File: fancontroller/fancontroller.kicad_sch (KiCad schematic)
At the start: 42 parts, among them J1 Power, J2 Serial Conn, M1 FAN0, M2 FAN0, M3 FAN0, M4 FAN0, M5 FAN0, M6 FAN0, Q1 AO3400A, Q10 AO3401A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

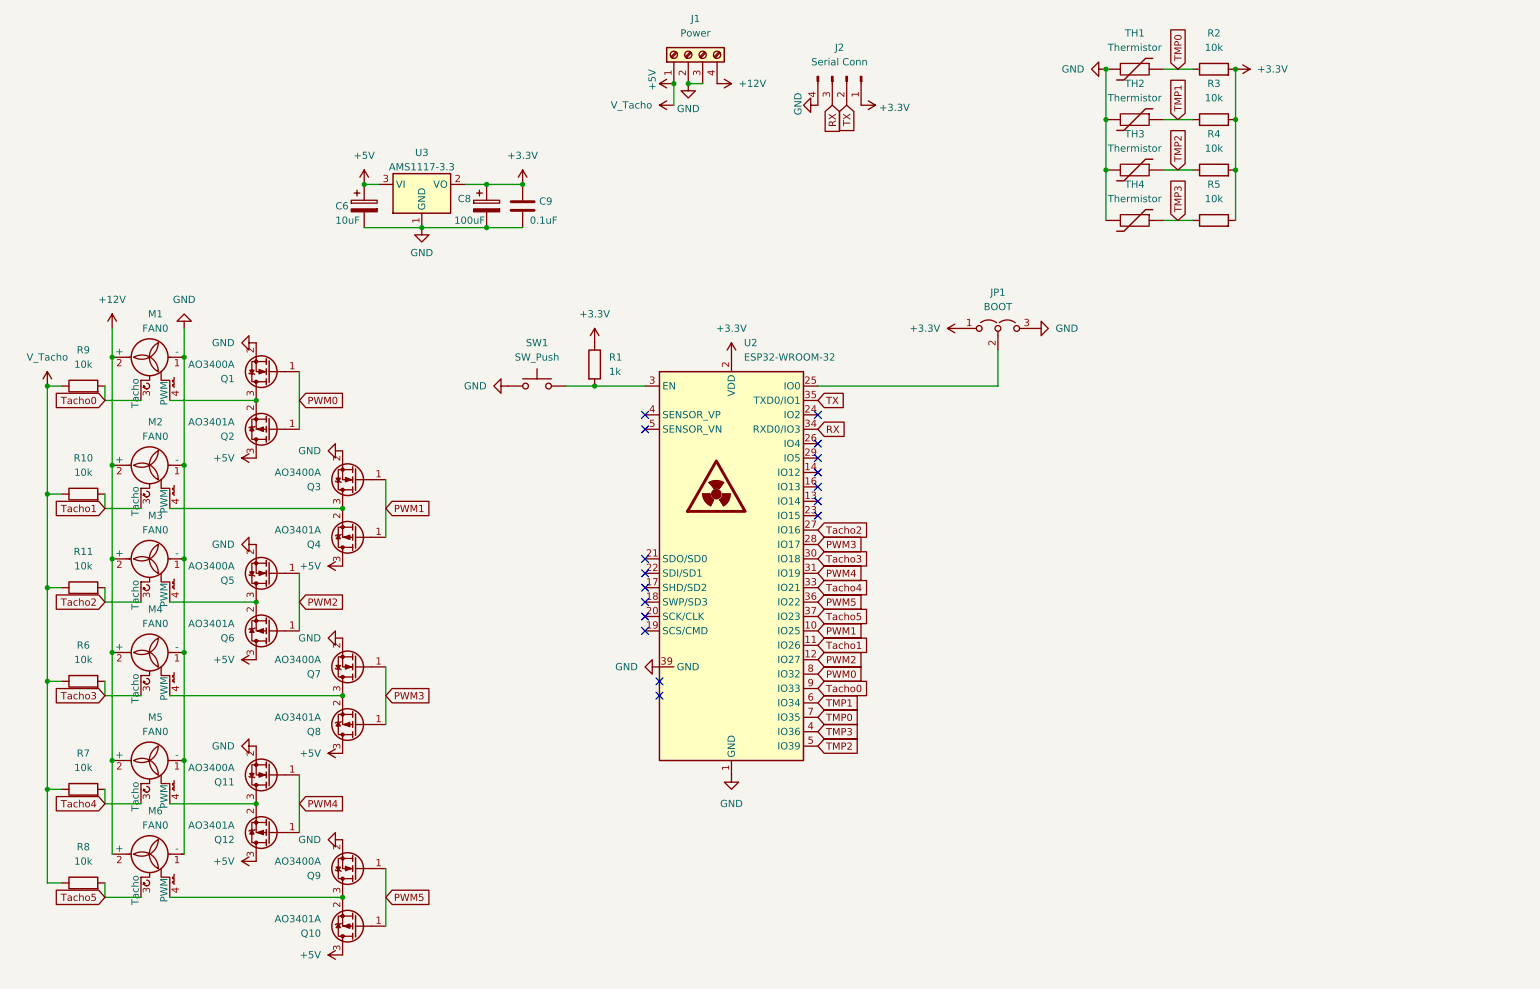
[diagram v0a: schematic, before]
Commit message: Break up into schematics and add USB-C programming interface
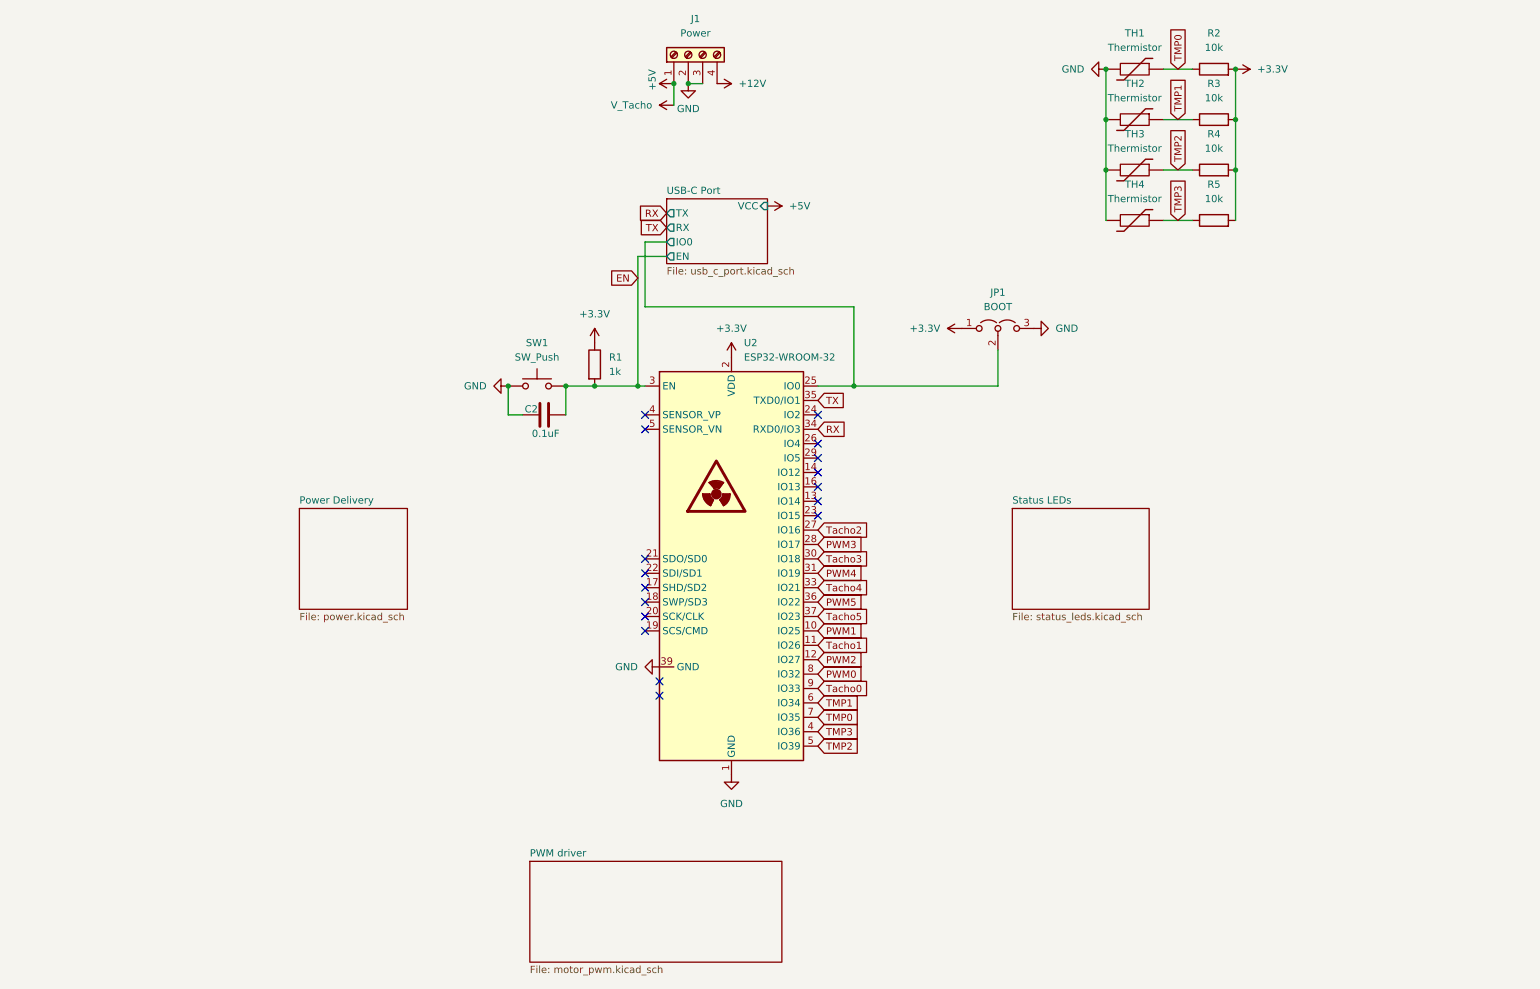
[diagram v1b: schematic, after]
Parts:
- removed C6: 10uF, Capacitor_SMD:C_0805_2012Metric, symbol Device:C_Polarized
- removed C8: 100uF, Capacitor_SMD:CP_Elec_10x10, symbol Device:C_Polarized
- removed C9: 0.1uF, Capacitor_SMD:C_0805_2012Metric, symbol Device:C
- removed J2: Serial Conn, Connector_PinHeader_2.54mm:PinHeader_1x04_P2.54mm_Horizontal, symbol Connector:Conn_01x04_Pin
- removed M1, M2, M3, M4, M5, M6: FAN0, Connector:FanPinHeader_1x04_P2.54mm_Vertical, symbol Motor:Fan_Tacho_PWM
- removed Q1, Q11, Q3, Q5, Q7, Q9: AO3400A, Package_TO_SOT_SMD:SOT-23, symbol Transistor_FET:AO3400A
- removed Q10, Q12, Q2, Q4, Q6, Q8: AO3401A, Package_TO_SOT_SMD:SOT-23, symbol Transistor_FET:AO3401A
- removed R10, R11, R6, R7, R8, R9: 10k, Resistor_SMD:R_0805_2012Metric, symbol Device:R
- removed U3: AMS1117-3.3, Package_TO_SOT_SMD:SOT-223-3_TabPin2, symbol Regulator_Linear:AMS1117-3.3
- added C2: 0.1uF, symbol Device:C
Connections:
- net GND: now also C2.2
- net EN: now reaches R1.2, SW1.2, U2.3 (EN)
- net EN: now also C2.1
- net USB-C Port/IO0: now reaches JP1.2 (C), U2.25 (IO0)
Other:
- added sheet PWM driver (motor_pwm.kicad_sch)
- added sheet Power Delivery (power.kicad_sch)
- added sheet Status LEDs (status_leds.kicad_sch)
- added sheet USB-C Port (usb_c_port.kicad_sch)

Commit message: Restructure Fan drivers into separate modules and rework USB-C
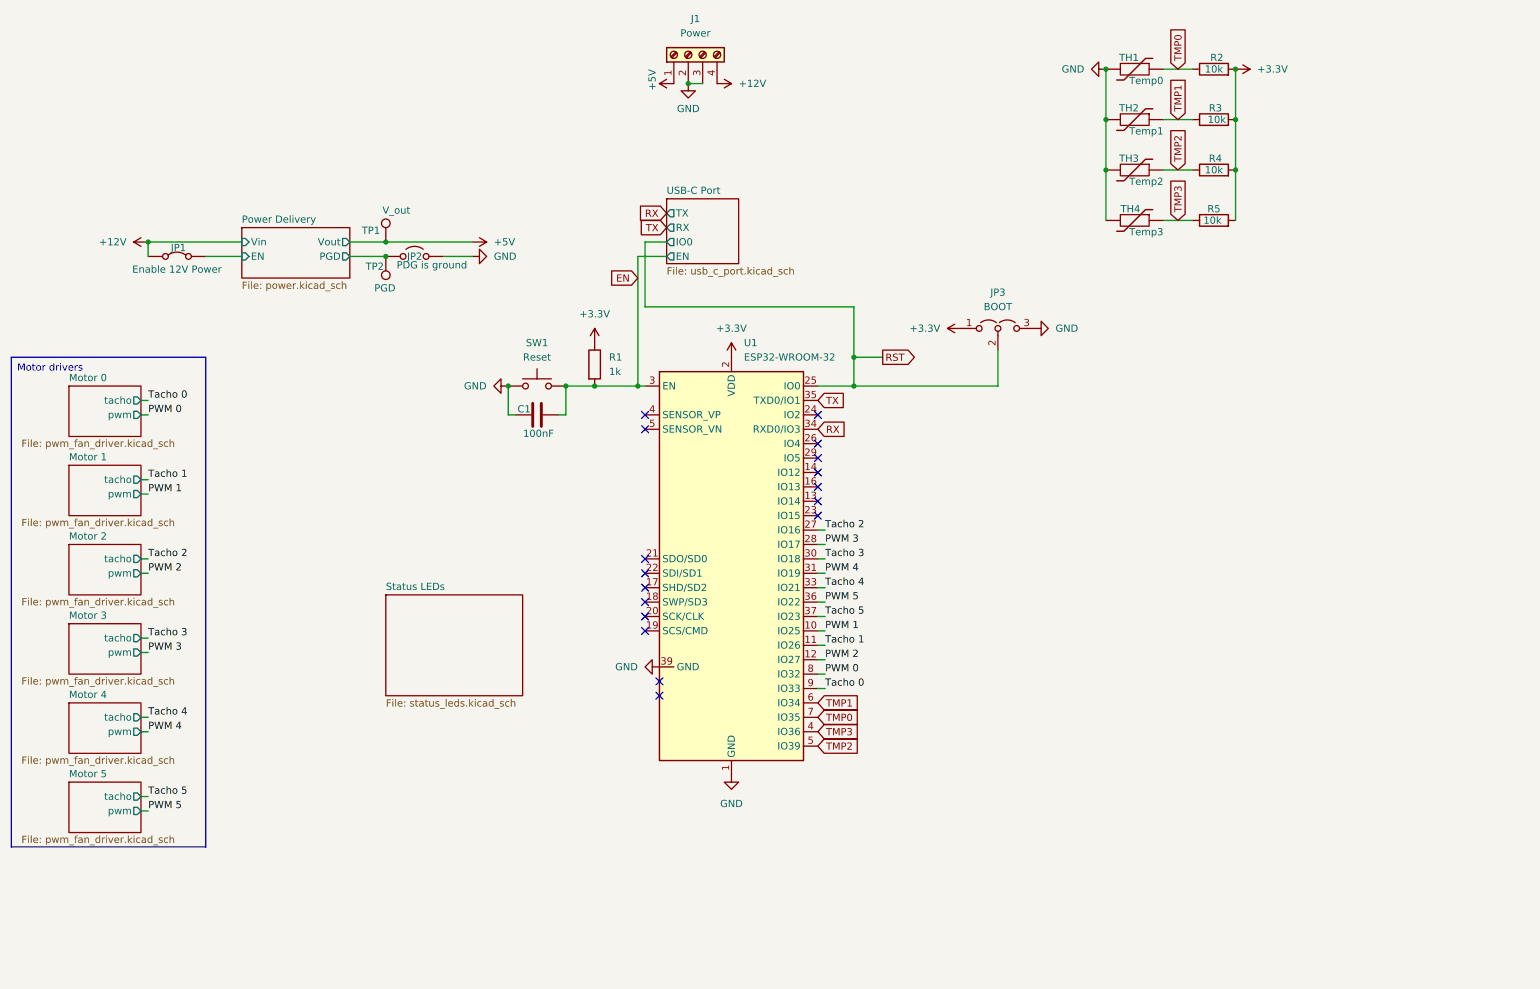
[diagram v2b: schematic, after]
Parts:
- added JP1: Enable 12V Power, symbol Jumper:Jumper_2_Bridged
- added JP2: PDG is ground, symbol Jumper:Jumper_2_Open
- added TP1: V_out, symbol Connector:TestPoint
- added TP2: PGD, symbol Connector:TestPoint
- C1: renamed from C2; value 0.1uF -> 100nF; footprint (none) -> Capacitor_SMD:C_0805_2012Metric; LCSC Part # (none) -> C1525
- SW1: value SW_Push -> Reset
- TH1: value Thermistor -> Temp0
- TH2: value Thermistor -> Temp1
- TH3: value Thermistor -> Temp2
- TH4: value Thermistor -> Temp3
- U1: renamed from U2; LCSC Part # (none) -> C2973652
- renumbered JP1 to JP3
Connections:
- net +12V: now also JP1.1 (A)
- net +5V: now also TP1.1
- net GND: now also JP2.2 (B)
- net PWM0 renamed PWM 0
- net PWM1 renamed PWM 1
- net PWM2 renamed PWM 2
- net PWM3 renamed PWM 3
- net PWM4 renamed PWM 4
- net PWM5 renamed PWM 5
- net Tacho0 renamed Tacho 0
- net Tacho1 renamed Tacho 1
- net Tacho2 renamed Tacho 2
- net Tacho3 renamed Tacho 3
- net Tacho4 renamed Tacho 4
- net Tacho5 renamed Tacho 5
- net USB-C Port/IO0 renamed RST
- new net Power Delivery/EN: JP1.2 (B)
- new net Power Delivery/PGD: JP2.1 (A), TP2.1
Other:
- removed sheet PWM driver
- added sheet Motor 0 (pwm_fan_driver.kicad_sch)
- added sheet Motor 1 (pwm_fan_driver.kicad_sch)
- added sheet Motor 2 (pwm_fan_driver.kicad_sch)
- added sheet Motor 3 (pwm_fan_driver.kicad_sch)
- added sheet Motor 4 (pwm_fan_driver.kicad_sch)
- added sheet Motor 5 (pwm_fan_driver.kicad_sch)
- sheet Power Delivery ports: added EN, PGD, Vin, Vout; removed none
- sheet USB-C Port ports: added none; removed VCC
- moved on the sheet: C1

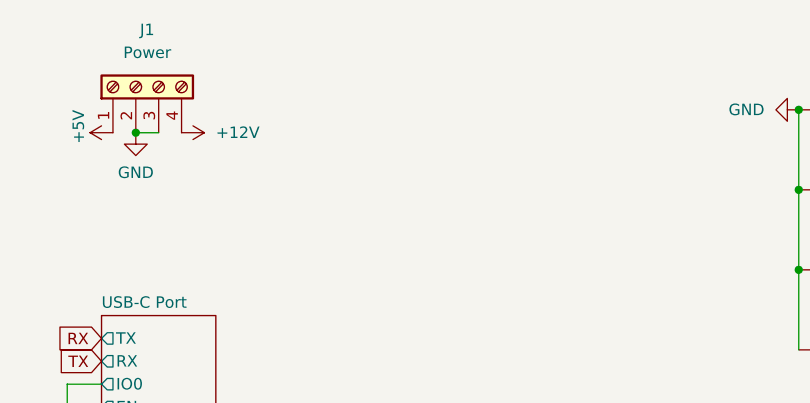
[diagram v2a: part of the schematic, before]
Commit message: Improve footprints and do massive overhaul for part numbering for better future order
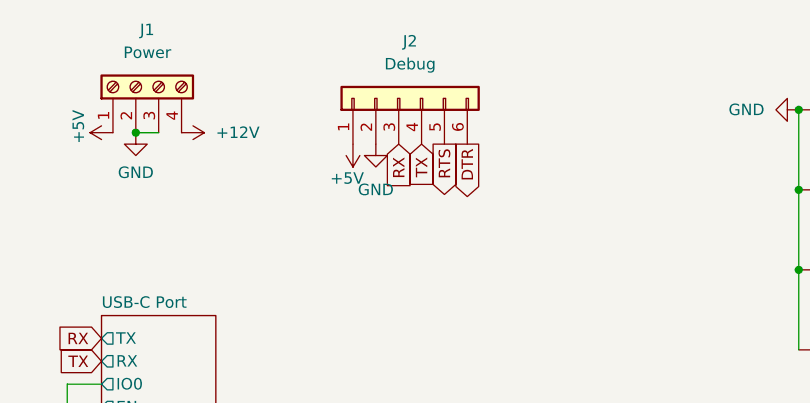
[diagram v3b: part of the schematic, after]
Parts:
- added J2: Debug, Connector_PinHeader_2.54mm:PinHeader_1x06_P2.54mm_Vertical, symbol Connector_Generic:Conn_01x06
- JP1, JP2: footprint (none) -> Connector_PinHeader_2.54mm:PinHeader_1x02_P2.54mm_Vertical
- TP1, TP2: footprint (none) -> TestPoint:TestPoint_Pad_2.5x2.5mm
- U1: footprint RF_Module:ESP32-WROOM-32 -> PCM_Espressif:ESP32-WROOM-32E
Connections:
- net +5V: now also J2.1 (Pin_1)
- net GND: now also J2.2 (Pin_2)
- net RX: now also J2.3 (Pin_3)
- net TX: now also J2.4 (Pin_4)
- new net DTR: J2.6 (Pin_6)
- new net RTS: J2.5 (Pin_5)
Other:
- company: (none) -> DJ-Bauer
- title: (none) -> ESP-Fancontroller

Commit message: Begin placing parts for v0.1 layout
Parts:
- J1: footprint Connector_PinHeader_2.54mm:PinHeader_1x04_P2.54mm_Horizontal -> Connector_PinHeader_2.54mm:PinHeader_1x04_P2.54mm_Vertical
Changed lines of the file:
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@@
 			)
 		)
-		(property "Footprint" "Connector_PinHeader_2.54mm:PinHeader_1x04_P2.54mm_Horizontal"
+		(property "Footprint" "Connector_PinHeader_2.54mm:PinHeader_1x04_P2.54mm_Vertical"
 			(at 133.35 29.21 0)
 			(effects

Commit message: edit schematic
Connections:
- net PWM 0: now also U1.12 (IO27); no longer U1.8 (IO32)
- net PWM 2: now also U1.8 (IO32); no longer U1.12 (IO27)
- net PWM 3: now also U1.36 (IO22); no longer U1.28 (IO17)
- net PWM 5: now also U1.27 (IO16); no longer U1.36 (IO22)
- net Tacho 0: now also U1.11 (IO26); no longer U1.9 (IO33)
- net Tacho 1: now also U1.9 (IO33); no longer U1.11 (IO26)
- net Tacho 2: now also U1.37 (IO23); no longer U1.27 (IO16)
- net Tacho 5: now also U1.28 (IO17); no longer U1.37 (IO23)
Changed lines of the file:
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@@
 	)
 	(label "Tacho 5"
-		(at 157.48 128.27 0)
+		(at 157.48 115.57 0)
 		(fields_autoplaced yes)
 		(effects
@@
 	)
 	(label "PWM 5"
-		(at 157.48 125.73 0)
+		(at 157.48 113.03 0)
 		(fields_autoplaced yes)
 		(effects
@@
 	)
 	(label "PWM 0"
-		(at 157.48 138.43 0)
+		(at 157.48 135.89 0)
 		(fields_autoplaced yes)
 		(effects
@@
 	)
 	(label "Tacho 2"
-		(at 157.48 113.03 0)
+		(at 157.48 128.27 0)
 		(fields_autoplaced yes)
 		(effects
@@
 	)
 	(label "PWM 3"
-		(at 157.48 115.57 0)
+		(at 157.48 125.73 0)
 		(fields_autoplaced yes)
 		(effects
@@
 	)
 	(label "PWM 2"
-		(at 157.48 135.89 0)
+		(at 157.48 138.43 0)
 		(fields_autoplaced yes)
 		(effects
@@
 	)
 	(label "Tacho 0"
-		(at 157.48 140.97 0)
+		(at 157.48 133.35 0)
 		(fields_autoplaced yes)
 		(effects
@@
 	)
 	(label "Tacho 1"
-		(at 157.48 133.35 0)
-		(fields_autoplaced yes)
-		(effects
+		(at 157.48 140.97 0)
+		(fields_autoplaced yes)
+		(effects

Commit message: Add i2c ADC
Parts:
- added C10: 10u, symbol Device:C
- added R27, R28: 10k, Resistor_SMD:R_0805_2012Metric, symbol Device:R
- added U5: ADS1115IDGS, Package_SO:TSSOP-10_3x3mm_P0.5mm, symbol Analog_ADC:ADS1115IDGS
- SW1: value Reset -> RESET
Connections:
- net +3.3V: now also C10.2, R27.1, R28.2, U5.8 (VDD)
- net GND: now also C10.1, U5.1 (ADDR), U5.3 (GND)
- net PWM 4: now also U1.27 (IO16); no longer U1.31 (IO19)
- net PWM 5: now also U1.31 (IO19); no longer U1.27 (IO16)
- net TMP0: now also U5.5 (AIN1); no longer U1.7 (IO35)
- net TMP1: now also U5.4 (AIN0); no longer U1.6 (IO34)
- net TMP2: now also U5.6 (AIN2); no longer U1.5 (SENSOR_VN)
- net TMP3: now also U5.7 (AIN3); no longer U1.4 (SENSOR_VP)
- net Tacho 3: now also U1.28 (IO17); no longer U1.30 (IO18)
- net Tacho 4: now also U1.30 (IO18); no longer U1.33 (IO21)
- net Tacho 5: now also U1.33 (IO21); no longer U1.28 (IO17)
- net SCL: now reaches U1.23 (IO15)
- net SCL: now also R28.1, U5.10 (SCL)
- net SDA: now reaches U1.24 (IO2)
- net SDA: now also R27.2, U5.9 (SDA)
- no-connect marks 17 -> 20
